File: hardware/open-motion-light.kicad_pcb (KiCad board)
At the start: 2 copper layers, 79 x 87 mm, 79 parts, among them J1 TYPE-C-31-M-12, J2 Conn_01x04, Q1 2N7002, SW1 SW_Push, SW2 SW_Push, SW3 SSSS213800, U1 CN3058E, U2 STM32L031G6U6, U3 MT9284BS6, U4 PIR223D-S0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

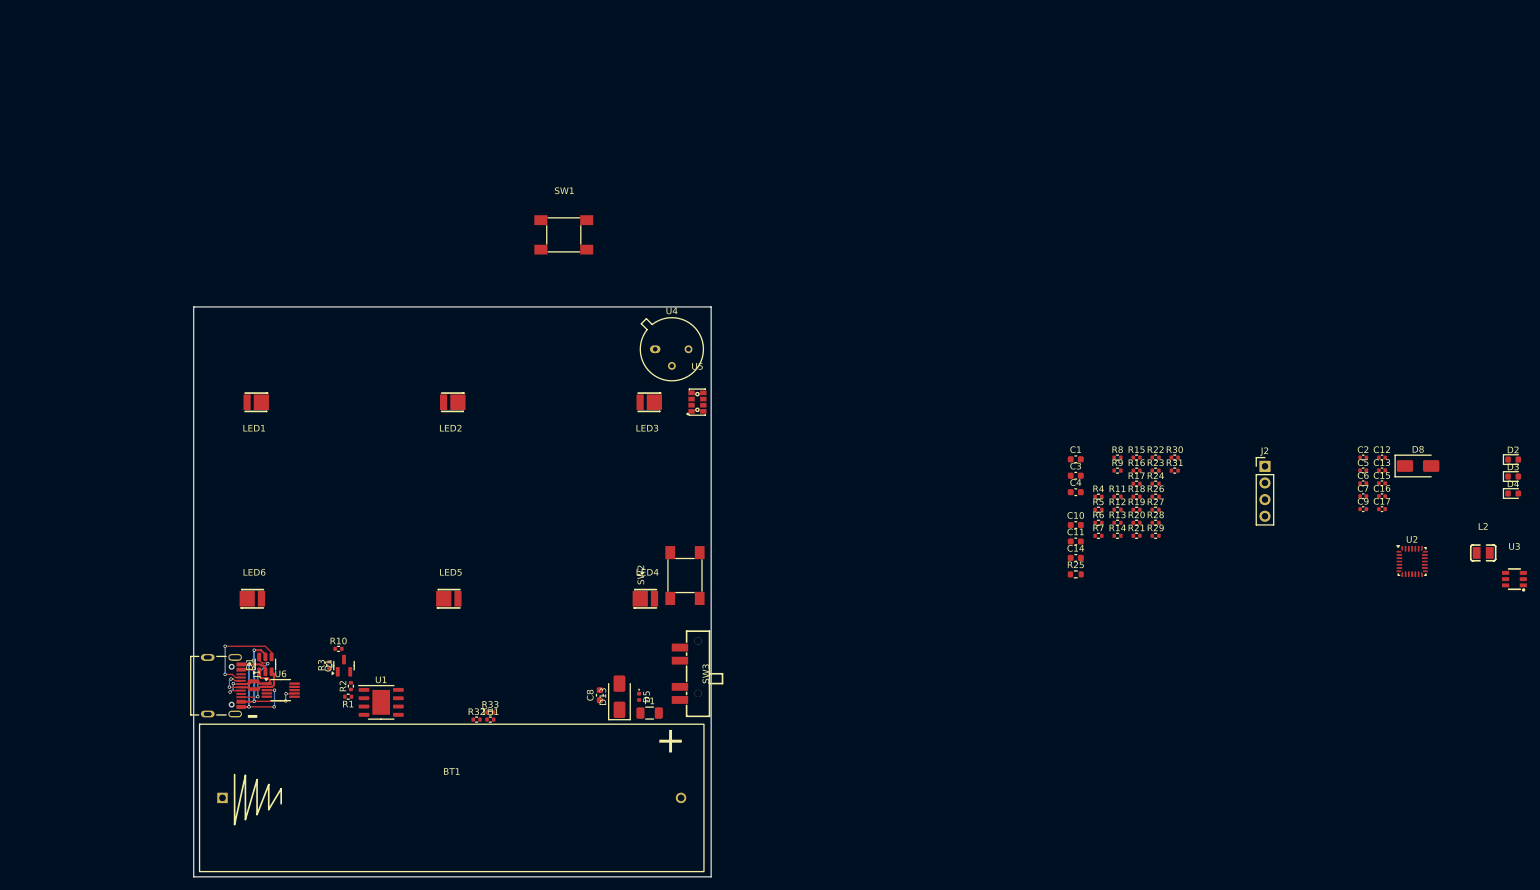
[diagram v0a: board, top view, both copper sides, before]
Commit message: Migrate three resistors to basic components, continue placement
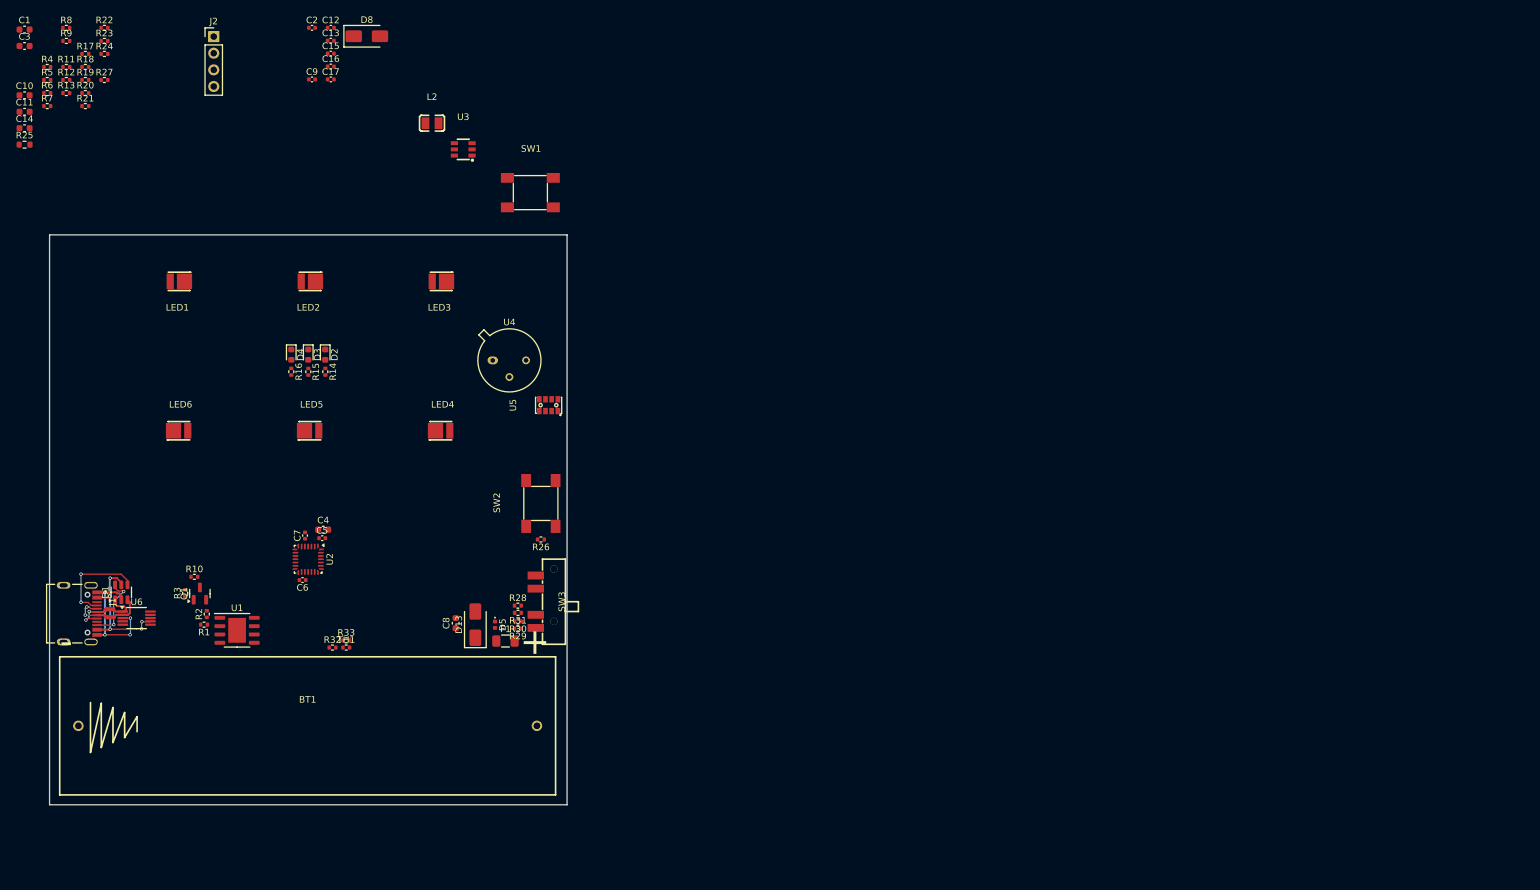
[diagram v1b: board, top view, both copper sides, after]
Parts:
- BT1: footprint Homebrew:BAT-TH_BH-18650-A1AJ005 -> easyeda2kicad:BAT-TH_BH-18650-A1AJ005
- moved D4 187.7 mm to (86.9, 68.3), turned to -90 degrees
- moved D3 184.9 mm to (89.5, 68.3), turned to -90 degrees
- moved D2 182.1 mm to (92.1, 68.3), turned to -90 degrees
- moved D8 173.4 mm to (98.4, 19.7)
- moved L2 173.4 mm to (108.4, 33.0)
- moved C1 173.4 mm to (46.2, 18.7)
- moved C10 173.4 mm to (46.2, 28.7)
- moved C11 173.4 mm to (46.2, 31.2)
- moved C12 173.4 mm to (92.9, 18.4)
- moved C13 173.4 mm to (92.9, 20.4)
- moved C14 173.4 mm to (46.2, 33.7)
- moved C15 173.4 mm to (92.9, 22.3)
- moved C16 173.4 mm to (92.9, 24.3)
- moved C17 173.4 mm to (92.9, 26.3)
- moved C2 173.4 mm to (90.1, 18.4)
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
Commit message: Continue placement
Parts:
- removed C14: 10uF, Capacitor_SMD:C_0603_1608Metric
- added C18: 100nF, Capacitor_SMD:C_0402_1005Metric, F.Cu at (121.3, 87.4)
- added C19: 47uF, Capacitor_SMD:C_1206_3216Metric, F.Cu at (119.6, 86.7)
- added C20: 10uF, Capacitor_SMD:C_0603_1608Metric, F.Cu at (127.1, 84.9)
- added H1: MountingHole, MountingHole:MountingHole_3.2mm_M3_ISO7380, F.Cu at (54.3, 66.3)
- added H2: MountingHole, MountingHole:MountingHole_3.2mm_M3_ISO7380, F.Cu at (124.7, 66.3)
- added H3: MountingHole, MountingHole:MountingHole_3.2mm_M3_ISO7380, F.Cu at (89.5, 109.6)
- added R34: 2Ω, Resistor_SMD:R_0603_1608Metric, F.Cu at (67.1, 81.8)
- added R35: 2M, Resistor_SMD:R_0603_1608Metric, F.Cu at (120.0, 104.8)
- added R36: 2M, Resistor_SMD:R_0603_1608Metric, F.Cu at (120.0, 99.6)
- added R37: 10, Resistor_SMD:R_0402_1005Metric, F.Cu at (124.3, 82.9)
- BT1: footprint easyeda2kicad:BAT-TH_BH-18650-A1AJ005 -> Homebrew:BAT-TH_BH-18650-A1AJ005
- C11: value 10uF -> 10uF 28V; footprint Capacitor_SMD:C_0603_1608Metric -> Capacitor_SMD:C_1206_3216Metric
- C13: value 100nF -> 47uF; footprint Capacitor_SMD:C_0402_1005Metric -> Capacitor_SMD:C_1206_3216Metric
- R1, R2: footprint Resistor_SMD:R_0402_1005Metric -> Resistor_SMD:R_0603_1608Metric
- R18: value 4k7 -> 100k
- R25: value 4.3Ω -> 2Ω
- R28, R29: value 3M3 -> 2M; footprint Resistor_SMD:R_0402_1005Metric -> Resistor_SMD:R_0603_1608Metric
- R33: value 360k -> 330k; footprint Resistor_SMD:R_0402_1005Metric -> Resistor_SMD:R_0603_1608Metric
- U5: value LTR-553ALS-01 -> VCNL4010-GS08; footprint easyeda2kicad:SENSOR-SMD_L3.9-W2.4-P0.95-BL -> easyeda2kicad:SENSORS-SMD_VCNL4010-GS08
- moved C3 98.7 mm to (83.9, 112.4)
- moved C1 97.3 mm to (74.1, 111.9), turned to 90 degrees
- moved R18 96.4 mm to (131.1, 84.1)
- moved R19 96.4 mm to (131.1, 86.1)
- moved R20 96.4 mm to (131.1, 88.1)
- moved R27 96.4 mm to (134.0, 86.1)
- moved R8 96.0 mm to (85.6, 108.5), turned to -90 degrees
- moved R9 93.2 mm to (83.5, 108.3), turned to -90 degrees
- moved R23 90.9 mm to (67.5, 110.8)
- moved R22 89.9 mm to (67.5, 107.8), turned to 180 degrees
- moved R6 88.4 mm to (84.0, 109.8), turned to 180 degrees
- moved R24 87.9 mm to (67.5, 109.8)
- moved R7 87.7 mm to (84.0, 111.0), turned to 180 degrees
- moved R17 84.7 mm to (117.5, 80.1), turned to 90 degrees
- moved R21 82.0 mm to (90.4, 104.5), turned to 90 degrees
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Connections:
- C12 pad 1: VCC -> GND
- C12 pad 2: GND -> Net-(U5-VDD)
- C13 pad 1: VCC -> GND
- C13 pad 2: GND -> VCC
- R18 pad 2: /SDA -> Net-(U5-INT)
- R20 pad 2: Net-(U5-INT) -> /SDA
- R25 pad 2: GND -> Net-(R25-Pad2)
- R28 pad 1: VCC -> Net-(R28-Pad1)
- R29 pad 2: VCC -> Net-(R29-Pad2)
- R8 pad 2: VCC -> Net-(U1-~{DONE})
- R9 pad 2: VCC -> Net-(U1-~{CHRG})
- U4 pad 1: (no net) -> VCC
- U4 pad 2: (no net) -> Net-(U4-RELOUT)
- U4 pad 3: (no net) -> GND
- U5 pad 1: /SDA -> VCC
- U5 pad 2: Net-(U5-INT) -> unconnected-(U5-IR_cathode-Pad2)
- U5 pad 3: Net-(U5-LDR) -> unconnected-(U5-IR_cathode-Pad3)
- U5 pad 4: Net-(U5-LDR) -> /SDA
- U5 pad 5: VCC -> /SCL
- U5 pad 6: GND -> Net-(U5-INT)
- U5 pad 7: /SCL -> Net-(U5-VDD)
- U5 pad 8: VCC -> unconnected-(U5-NC-Pad8)
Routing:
- net VCC: track 0.00 -> 12.6 mm
- net GND: track 19.9 -> 32.0 mm
- net Net-(D8-A): track 0.00 -> 9.95 mm, vias 0 -> 2
- net Net-(D8-K): track 0.00 -> 6.66 mm
- net Net-(U3-FB): track 0.00 -> 4.76 mm
- net Net-(R25-Pad2): track 0.00 -> 1.42 mm
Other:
- board size 79 x 87 mm -> 77 x 73 mm

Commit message: Finish placement
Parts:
- L2: footprint easyeda2kicad:L0806 -> Homebrew:L0806
- LED1, LED2, LED3, LED4, LED5, LED6: footprint easyeda2kicad:LED-SMD_L3.3-W2.8-RD -> Homebrew:LED-SMD_L3.3-W2.8-RD
- SW3: footprint easyeda2kicad:SW-SMD_SSSS213800 -> Homebrew:SW-SMD_SSSS213800
- U3: footprint easyeda2kicad:SOT-23-6_L2.9-W1.6-P0.95-LS2.8-BR -> Homebrew:SOT-23-6_L2.9-W1.6-P0.95-LS2.8-BR
- U5: footprint easyeda2kicad:SENSORS-SMD_VCNL4010-GS08 -> Homebrew:SENSORS-SMD_VCNL4010-GS08
- moved C2 70.4 mm to (60.4, 111.9), turned to 180 degrees
- moved C15 61.5 mm to (64.7, 106.1), turned to 180 degrees
- moved C16 58.5 mm to (66.4, 105.7), turned to 90 degrees
- moved R13 57.8 mm to (108.4, 93.4), turned to 180 degrees
- moved J2 46.7 mm to (101.3, 96.1)
- moved C17 41.9 mm to (80.3, 96.7)
- moved R4 19.8 mm to (64.7, 103.8)
- moved R5 16.4 mm to (62.2, 101.3)
- moved R12 16.2 mm to (64.7, 102.8)
- moved R27 16.2 mm to (118.3, 89.9), turned to 180 degrees
- moved R11 13.2 mm to (62.2, 100.3), turned to 180 degrees
- moved R18 8.50 mm to (126.4, 91.2), turned to 90 degrees
- moved R19 7.72 mm to (125.3, 91.2), turned to 90 degrees
- moved R20 7.57 mm to (124.2, 91.2), turned to 90 degrees
- moved R10 1.09 mm to (70.7, 105.0)
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
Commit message: First pass at routing
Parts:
- added C14: 100nF, Capacitor_SMD:C_0402_1005Metric, F.Cu at (123.2, 71.3)
- moved R18 3.86 mm to (122.6, 90.5)
- moved R19 1.30 mm to (124.8, 92.4), turned to 0 degrees
- moved C2 1.03 mm to (60.5, 110.9), turned to -90 degrees
- moved R6 0.80 mm to (84.0, 109.0)
- moved R7 0.80 mm to (84.0, 110.2)
- moved R9 0.80 mm to (83.5, 107.5)
- moved R30 0.71 mm to (119.4, 107.7)
- moved R21 0.62 mm to (90.5, 103.9)
- moved R8 0.40 mm to (85.6, 108.1)
- moved D5 0.22 mm to (116.8, 109.6)
- moved R20 0.14 mm to (124.1, 91.3), turned to 0 degrees
- turned R22 to 0 degrees
- turned R26 to 0 degrees
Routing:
- net VCC: track 12.6 -> 277.6 mm, vias 0 -> 10
- net GND: track 32.0 -> 104.4 mm, vias 4 -> 104
- net /PIR: track 0.00 -> 48.8 mm, vias 0 -> 2
- net /WHITE_LED: track 0.00 -> 48.3 mm, vias 0 -> 2
- net /SDA: track 0.00 -> 47.3 mm, vias 0 -> 2
- net /POWER_AUTO: track 0.00 -> 46.4 mm, vias 0 -> 2
- net /SCL: track 0.00 -> 45.9 mm, vias 0 -> 2
- net /LIGHT_INT: track 0.00 -> 45.1 mm, vias 0 -> 2
- net Net-(U2-NRST): track 0.00 -> 42.4 mm, vias 0 -> 4
- net /BUTTON: track 0.00 -> 42.4 mm, vias 0 -> 4
- net /POWER_ON: track 0.00 -> 38.5 mm, vias 0 -> 4
- net /BOOT0: track 0.00 -> 33.9 mm, vias 0 -> 2
- net /CC1: track 0.00 -> 32.1 mm, vias 0 -> 2
- net /TEMP: track 0.00 -> 31.7 mm, vias 0 -> 2
- net /CC2: track 0.00 -> 30.1 mm, vias 0 -> 2
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- added copper zone on B.Cu, net GND
- added copper zone on F.Cu, net GND

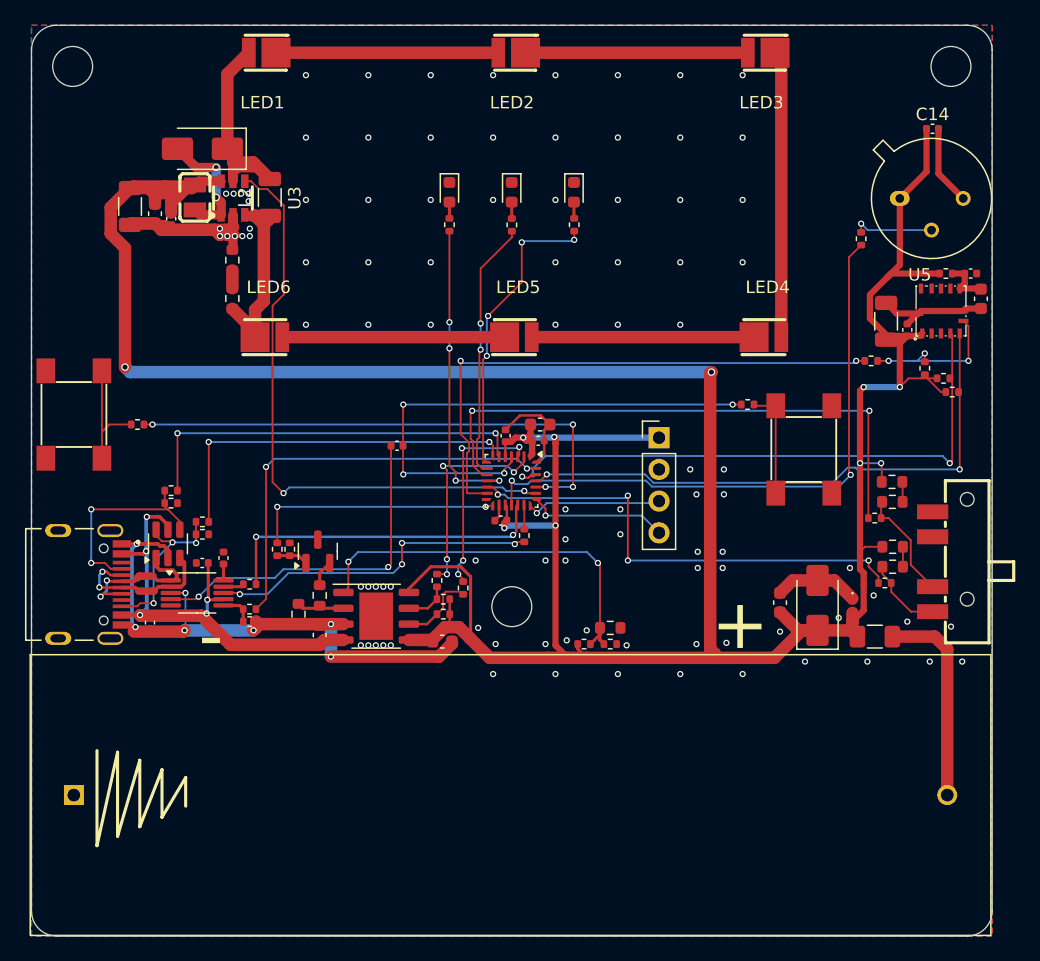
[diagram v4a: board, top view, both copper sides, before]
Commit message: Add lots of stitching vias
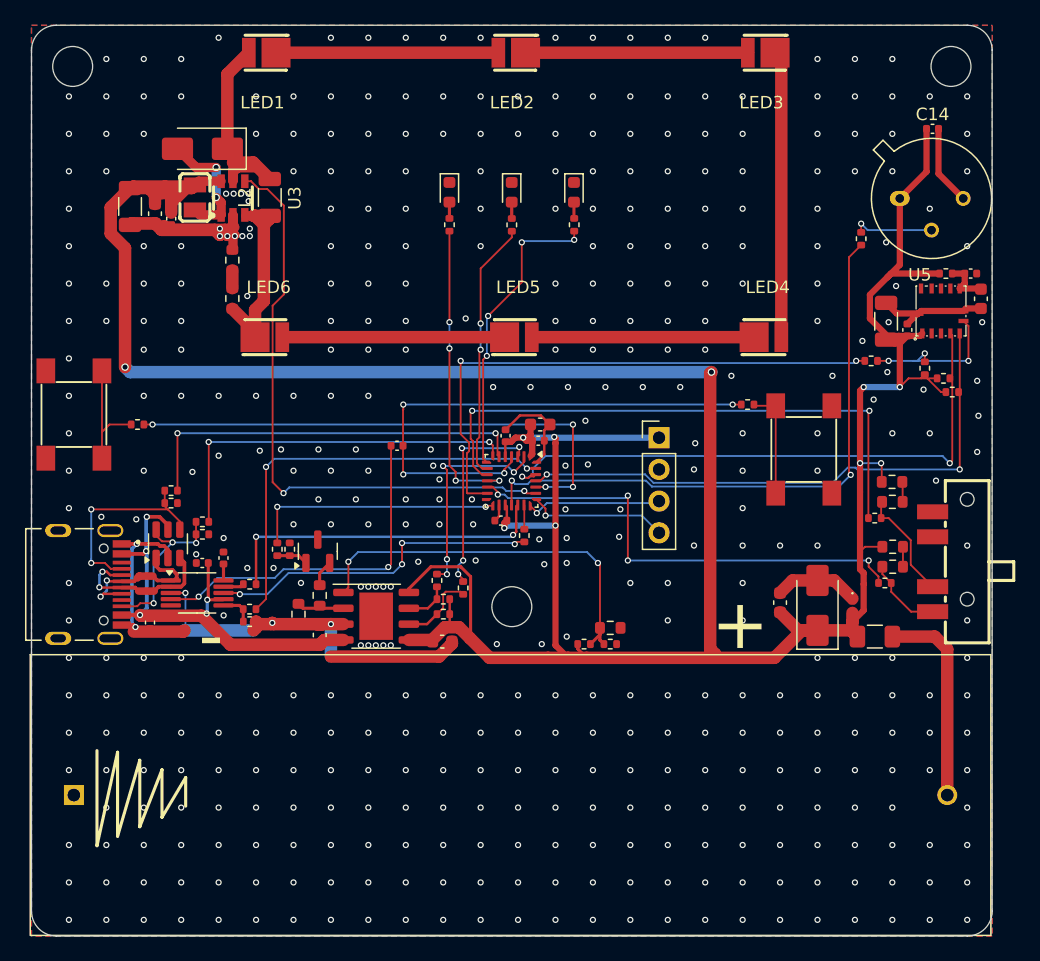
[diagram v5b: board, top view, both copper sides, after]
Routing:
- net GND: track 104.4 -> 104.5 mm, vias 104 -> 453
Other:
- board text added: "{ "ViaStitching": "0.2", "stitch_zone_0": { "HSpacing": "5", "VSpacing": "5", "Clearance": "0.5", "Randomize": false } }"

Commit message: Hardware revision v1.0
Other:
- board text added: "+"
- board text added: "-"
- board text added: "BATTERY"
- board text added: "GND"
- board text added: "LIGHT"
- board text added: "M3 x3"
- board text added: "PIR"
- board text added: "RESET"
- board text added: "SW1"
- board text added: "SWCLK"
- board text added: "SWDIO"
- board text added: "VCC"
- board text added: "open-motion-light v1.0"
